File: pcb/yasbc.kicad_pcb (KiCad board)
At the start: 4 copper layers, 100 x 100 mm, 209 parts, among them J1 USB TTY, J10 AudioJack3, J11 Conn_02x20_Odd_Even, J2 HDMI_A, J3 USB DEV, J4 1V5, J5 1V5, J6 USB HOST, J7 1V5, J8 1V5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

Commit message: WIP
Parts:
- moved C79 8.70 mm to (62.7, -58.0)
- moved C80 8.70 mm to (64.1, -56.7)
- moved R42 8.70 mm to (63.2, -59.3)
- moved R43 8.70 mm to (65.4, -57.2)
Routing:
- net /DDR3_ODT: track 3.34 -> 45.3 mm
- net /DDR3_RST: track 1.62 -> 37.5 mm
- net /DDR3_A2: track 0.00 -> 33.7 mm
- net /DDR3_BA0: track 0.00 -> 33.5 mm
- net /DDR3_WE: track 0.00 -> 33.0 mm, vias 0 -> 2
- net /DDR3_D14: track 0.00 -> 33.0 mm, vias 0 -> 3
- net /DDR3_CAS: track 0.00 -> 32.7 mm, vias 0 -> 2
- net /DDR3_RAS: track 0.00 -> 32.5 mm, vias 0 -> 2
- net /DDR3_BA2: track 0.00 -> 31.7 mm
- net /DDR3_A0: track 1.74 -> 33.1 mm
- net /DDR3_D12: track 4.90 -> 33.3 mm, vias 1 -> 2
- net /DDR3_D10: track 0.00 -> 22.6 mm, vias 0 -> 1
- net /DDR3_D7: track 1.56 -> 23.4 mm, vias 1 -> 2
- net /DDR3_DQS0+: track 24.7 -> 4.42 mm
- net /DDR3_DQS0-: track 23.7 -> 3.85 mm
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- added copper zone on B.Cu, net +1V5

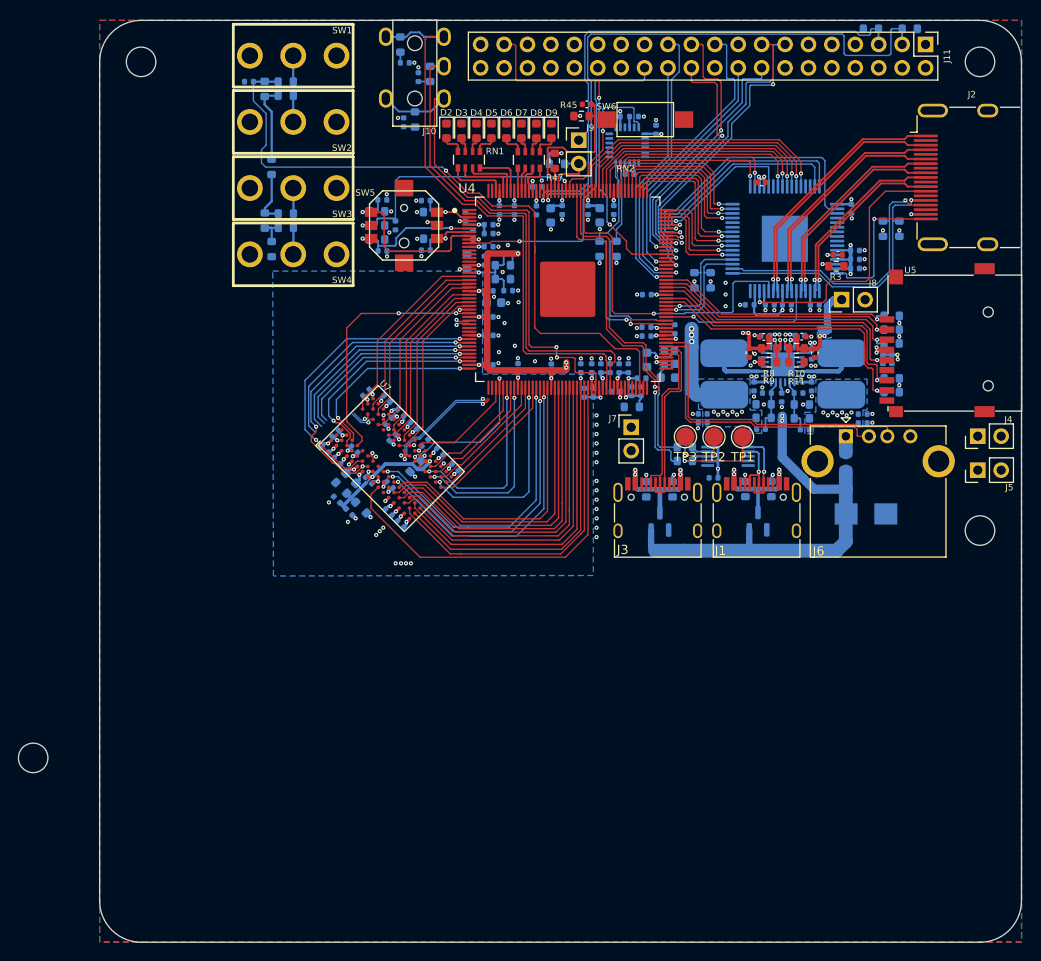
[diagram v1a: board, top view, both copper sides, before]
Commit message: DDR3 clock, address and control routing
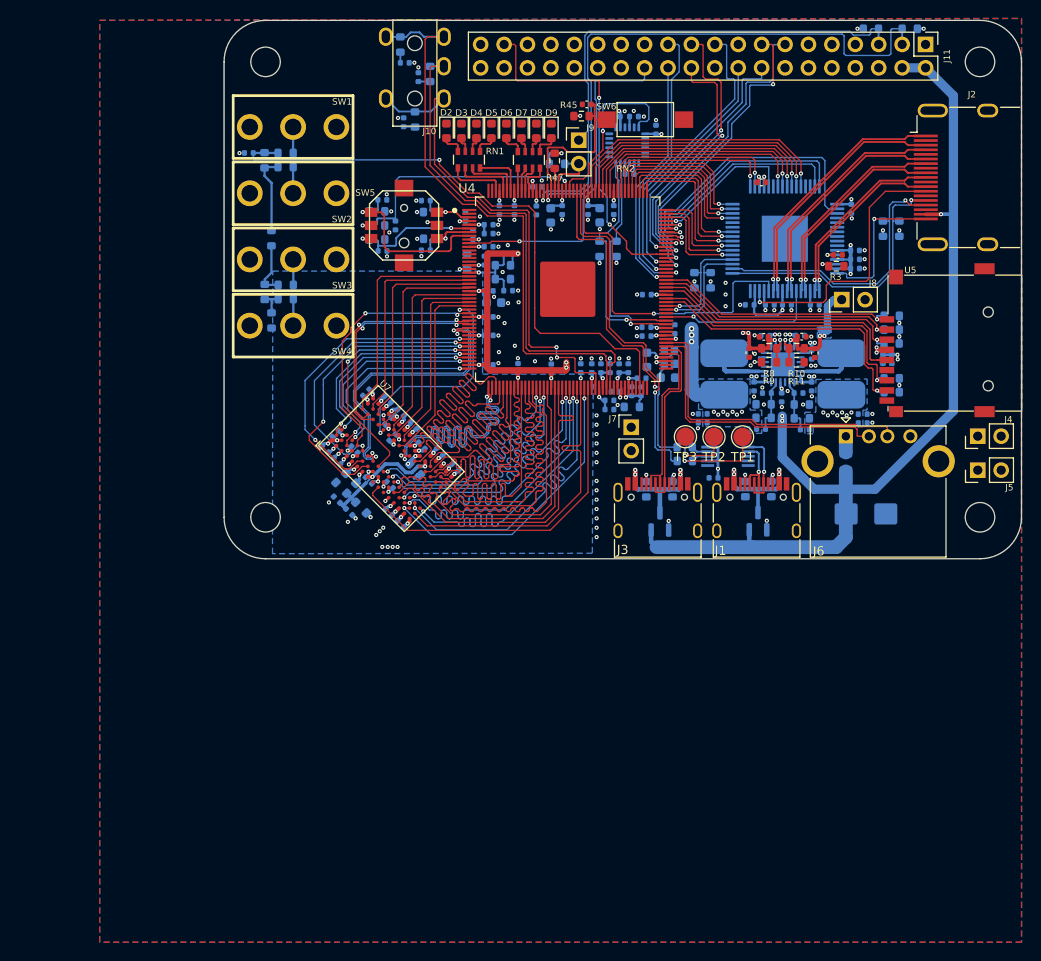
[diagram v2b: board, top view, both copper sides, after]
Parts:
- moved H4 36.3 mm to (55.0, -56.1)
- moved H3 13.5 mm to (55.0, -105.5)
- moved R20 7.74 mm to (54.9, -94.8)
- moved SW2 7.74 mm to (58.0, -91.2)
- moved C33 7.74 mm to (53.2, -95.6)
- moved R16 7.74 mm to (57.2, -95.6)
- moved R17 7.74 mm to (57.2, -94.1)
- moved R18 7.74 mm to (57.2, -81.3)
- moved R19 7.74 mm to (57.2, -79.8)
- moved R21 7.74 mm to (55.6, -86.4)
- moved R22 7.74 mm to (54.9, -80.5)
- moved R23 7.74 mm to (55.7, -77.5)
- moved SW1 7.74 mm to (58.0, -98.4)
- moved SW3 7.74 mm to (58.0, -84.1)
- moved SW4 7.74 mm to (58.0, -76.9)
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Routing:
- net /DDR3_DQS1+: track 0.76 -> 31.1 mm, vias 1 -> 2
- net /DDR3_DQS1-: track 0.76 -> 30.9 mm, vias 1 -> 2
- net +5V: track 101.6 -> 125.1 mm, vias 10 -> 11
- net /DDR3_DM1: track 1.05 -> 24.2 mm, vias 1 -> 2
- net /DDR3_CKE: track 11.7 -> 34.6 mm
- net /DDR3_BA1: track 12.9 -> 34.6 mm
- net /DDR3_A8: track 14.1 -> 35.0 mm
- net /DDR3_A6: track 13.8 -> 34.3 mm
- net /DDR3_CK-: track 13.5 -> 33.7 mm
- net /DDR3_CK+: track 13.5 -> 33.7 mm
- net /DDR3_DQS0+: track 4.42 -> 24.4 mm
- net /DDR3_DQS0-: track 3.85 -> 23.3 mm
- net /DDR3_A4: track 13.3 -> 32.5 mm
- net /DDR3_A14: track 15.7 -> 34.0 mm
- net /DDR3_A10: track 16.2 -> 32.3 mm, vias 2 -> 0
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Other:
- board size 100 x 100 mm -> 86.5 x 58.4 mm
